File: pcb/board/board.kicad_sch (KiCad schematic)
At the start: 132 parts, among them J1 (A) USB_C_Receptacle_USB2.0_1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, J10 OLED_128x32, J11 LCD_128x160, J12 AudioJack3, J13 Conn_01x02, J14 Micro_SD_Card, J15 Conn_01x03, J16 Conn_01x06, J17 Conn_01x03, J18 Conn_01x03, J19 Conn_01x03, J2 (B) USB_C_Receptacle_USB2.0_1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, J20 Conn_01x04, J21 Conn_01x04, J22 Conn_01x05, J23 Conn_01x05, J24 Conn_01x05, J25 Conn_01x02, J3 (C) USB_C_Receptacle_USB2.0_1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, J4 Conn_01x03, J5 Conn_01x03, J6 Conn_01x04, J7 Conn_01x07, J8 Conn_01x04, J9 Conn_01x02, SW1 SW_Push, SW2 SW_Push, SW3 Switch, SW4 Switch, SW5 Switch, SW6 RotaryEncoder_Switch, U1 RP2040, U2 NCP1117-3.3_SOT223, U3 W25Q16JVZPIQ TR, U4 NCP1117-3.3_SOT223, U5 RP2040, U6 W25Q16JVZPIQ TR, U7 PCM5101A, U8 TLV70033_SOT23-5, U9 TPA6132A2RTE, Y1 12MHz, Y2 12MHz

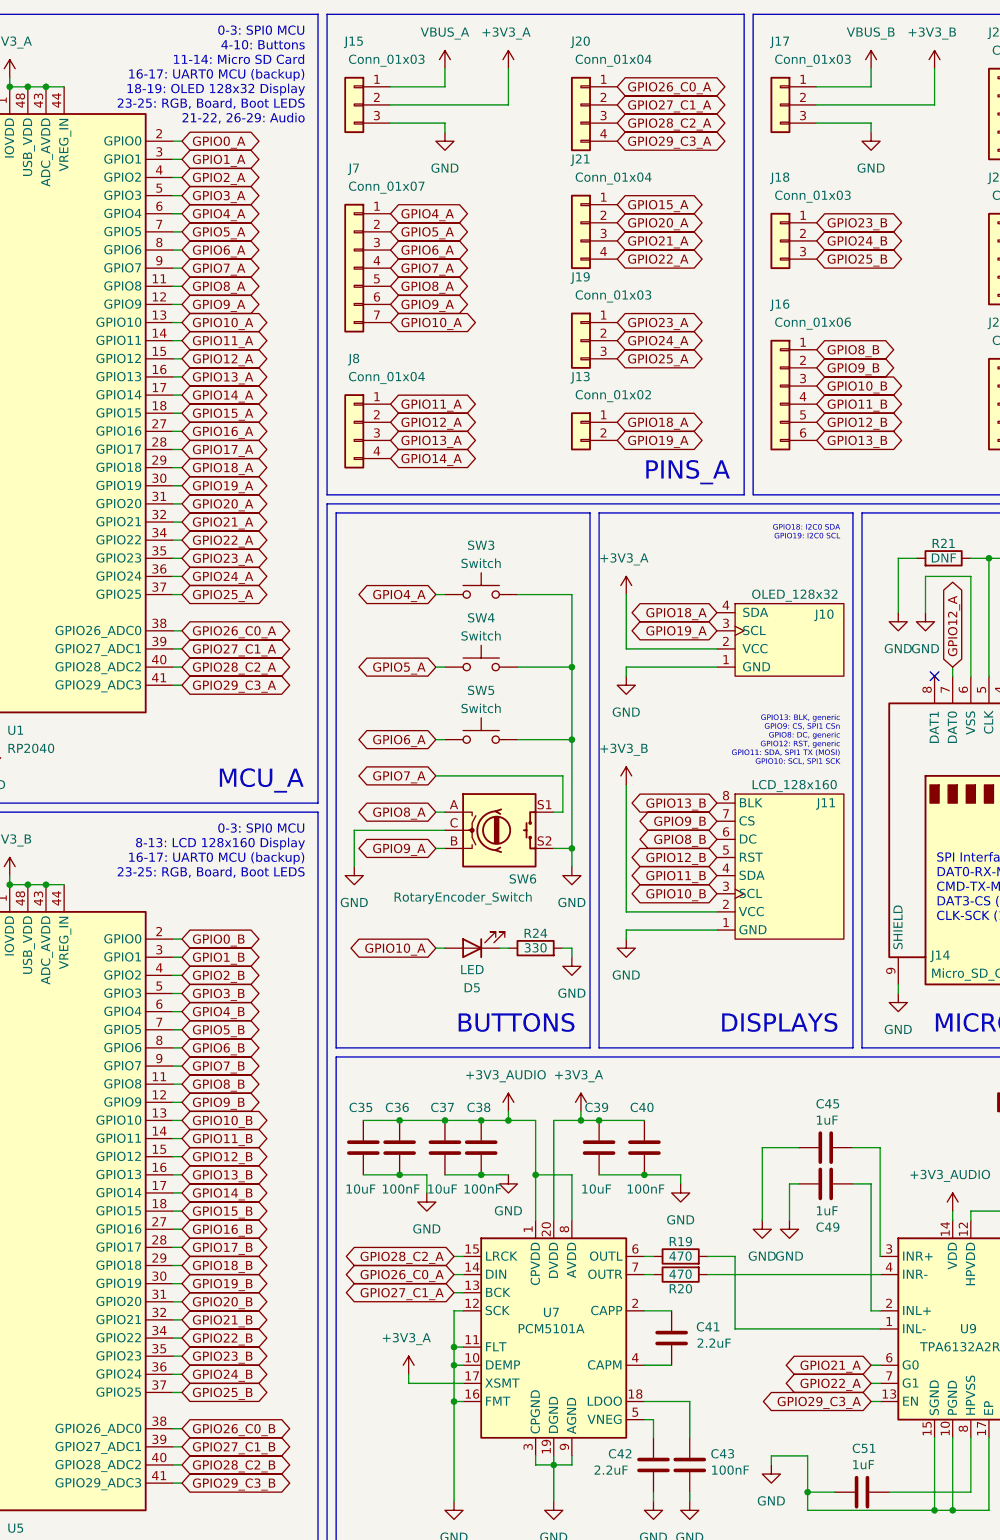
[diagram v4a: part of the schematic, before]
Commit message: 08172026 - pcb work continues! (audio and most mcu pin connections!)
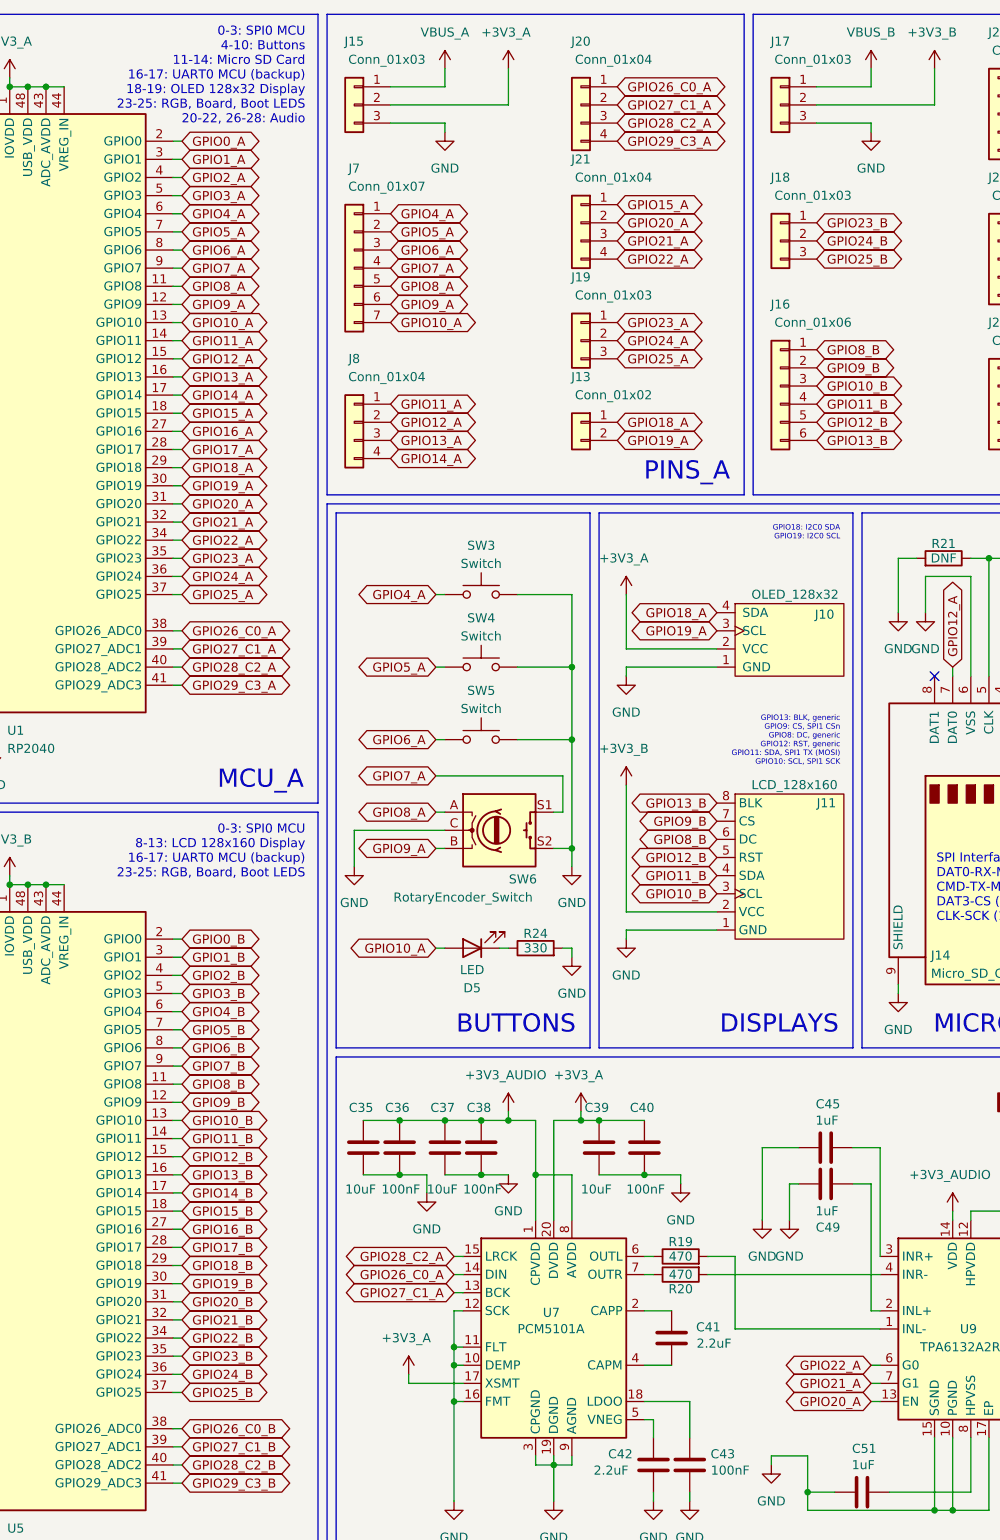
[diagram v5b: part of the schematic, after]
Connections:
- net GPIO20_A: now also U9.13 (EN)
- net GPIO21_A: now also U9.7 (G1); no longer U9.6 (G0)
- net GPIO22_A: now also U9.6 (G0); no longer U9.7 (G1)
- net GPIO29_C3_A: no longer U9.13 (EN)
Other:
- note added: "0-3: SPI0 MCU 4-10: Buttons 11-14: Micro SD Card 16-17: UART0 MCU (backup) 18-19: OLED 128x32 Display 23-25: RGB, Board, Boot LEDS 20-22, 26-28: Audio"
- note removed: "0-3: SPI0 MCU 4-10: Buttons 11-14: Micro SD Card 16-17: UART0 MCU (backup) 18-19: OLED 128x32 Display 23-25: RGB, Board, Boot LEDS 21-22, 26-29: Audio"
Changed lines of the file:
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@@
 	(wire
 		(pts
+			(xy 363.22 204.47) (xy 364.49 204.47)
+		)
+		(stroke
+			(width 0)
+			(type default)
+		)
+	)
+	(wire
+		(pts
 			(xy 163.83 144.78) (xy 170.18 144.78)
 		)
@@
 	(wire
 		(pts
+			(xy 363.22 207.01) (xy 364.49 207.01)
+		)
+		(stroke
+			(width 0)
+			(type default)
+		)
+	)
+	(wire
+		(pts
 			(xy 321.31 217.17) (xy 321.31 218.44)
 		)
@@
 	(wire
 		(pts
-			(xy 363.22 207.01) (xy 364.49 207.01)
-		)
-		(stroke
-			(width 0)
-			(type default)
-		)
-	)
-	(wire
-		(pts
 			(xy 69.85 144.78) (xy 69.85 143.51)
 		)
@@
 	(wire
 		(pts
-			(xy 363.22 204.47) (xy 364.49 204.47)
-		)
-		(stroke
-			(width 0)
-			(type default)
-		)
-	)
-	(wire
-		(pts
 			(xy 213.36 99.06) (xy 214.63 99.06)
 		)
@@
 		)
 	)
-	(text "0-3: SPI0 MCU\n4-10: Buttons\n11-14: Micro SD Card\n16-17: UART0 MCU (backup)\n18-19: OLED 128x32 Display\n23-25: RGB, Board, Boot LEDS\n21-22, 26-29: Audio"
+	(text "0-3: SPI0 MCU\n4-10: Buttons\n11-14: Micro SD Card\n16-17: UART0 MCU (backup)\n18-19: OLED 128x32 Display\n23-25: RGB, Board, Boot LEDS\n20-22, 26-28: Audio"
 		(exclude_from_sim no)
 		(at 283.972 17.018 0)
@@
 	(global_label "GPIO21_A"
 		(shape bidirectional)
-		(at 363.22 204.47 180)
+		(at 363.22 207.01 180)
 		(fields_autoplaced yes)
 		(effects
@@
 		)
 		(property "Intersheetrefs" "${INTERSHEET_REFS}"
-			(at 350.173 204.47 0)
+			(at 350.173 207.01 0)
 			(effects
 				(font
@@
 		)
 	)
+	(global_label "GPIO20_A"
+		(shape bidirectional)
+		(at 363.22 209.55 180)
+		(fields_autoplaced yes)
+		(effects
+			(font
+				(size 1.27 1.27)
+			)
+			(justify right)
+		)
+		(property "Intersheetrefs" "${INTERSHEET_REFS}"
+			(at 350.173 209.55 0)
+			(effects
+				(font
+					(size 1.27 1.27)
+				)
+				(justify right)
+				(hide yes)
+			)
+		)
+	)
 	(global_label "GPIO22_A"
 		(shape bidirectional)
@@
 		)
 	)
-	(global_label "GPIO29_C3_A"
-		(shape bidirectional)
-		(at 363.22 209.55 180)
-		(fields_autoplaced yes)
-		(effects
-			(font
-				(size 1.27 1.27)
-			)
-			(justify right)
-		)
-		(property "Intersheetrefs" "${INTERSHEET_REFS}"
-			(at 346.7259 209.55 0)
-			(effects
-				(font
-					(size 1.27 1.27)
-				)
-				(justify right)
-				(hide yes)
-			)
-		)
-	)
 	(global_label "GPIO7_B"
 		(shape bidirectional)
@@
 	(global_label "GPIO22_A"
 		(shape bidirectional)
-		(at 363.22 207.01 180)
+		(at 363.22 204.47 180)
 		(fields_autoplaced yes)
 		(effects
@@
 		)
 		(property "Intersheetrefs" "${INTERSHEET_REFS}"
-			(at 350.173 207.01 0)
+			(at 350.173 204.47 0)
 			(effects
 				(font

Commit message: leds and more connections!
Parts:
- removed J13: Conn_01x02, Connector_PinHeader_2.54mm:PinHeader_1x02_P2.54mm_Vertical, symbol Connector_Generic:Conn_01x02
- removed J15, J17, J18, J19: Conn_01x03, Connector_PinHeader_2.54mm:PinHeader_1x03_P2.54mm_Vertical, symbol Connector_Generic:Conn_01x03
- removed J16: Conn_01x06, Connector_PinHeader_2.54mm:PinHeader_1x06_P2.54mm_Vertical, symbol Connector_Generic:Conn_01x06
- removed J20, J21, J8: Conn_01x04, Connector_PinHeader_2.54mm:PinHeader_1x04_P2.54mm_Vertical, symbol Connector_Generic:Conn_01x04
- removed J22, J23, J24: Conn_01x05, Connector_PinHeader_2.54mm:PinHeader_1x05_P2.54mm_Vertical, symbol Connector_Generic:Conn_01x05
- removed J7: Conn_01x07, Connector_PinHeader_2.54mm:PinHeader_1x07_P2.54mm_Vertical, symbol Connector_Generic:Conn_01x07
- added J13, J7: Conn_01x01, TestPoint:TestPoint_Pad_1.0x1.0mm, symbol Connector_Generic:Conn_01x01
- added J15, J16, J8: Conn_01x01, Connector_PinHeader_2.54mm:PinHeader_1x01_P2.54mm_Vertical, symbol Connector_Generic:Conn_01x01
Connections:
- net +3V3_A: now also J8.1 (Pin_1)
- net +3V3_B: now also J15.1 (Pin_1)
- net GND: now also J16.1 (Pin_1)
- net VBUS_A: now also J7.1 (Pin_1)
- net VBUS_B: now also J13.1 (Pin_1)

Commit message: 08192026 - starting to wrap up pcb work!
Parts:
- removed J25, J9: Conn_01x02, Connector_PinHeader_2.54mm:PinHeader_1x02_P2.54mm_Vertical, symbol Connector_Generic:Conn_01x02
- removed J6: Conn_01x04, Connector_PinHeader_2.54mm:PinHeader_1x04_P2.54mm_Vertical, symbol Connector_Generic:Conn_01x04
- added J17, J18, J19, J20, J21, J22, J6, J9: Conn_01x01, TestPoint:TestPoint_Pad_D1.0mm, symbol Connector_Generic:Conn_01x01
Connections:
- net GPIO0_A: now also J6.1 (Pin_1)
- net GPIO0_B: now also J19.1 (Pin_1)
- net GPIO16_A: now also J9.1 (Pin_1)
- net GPIO16_B: now also J22.1 (Pin_1)
- net GPIO1_A: now also J17.1 (Pin_1)
- net GPIO2_A: now also J18.1 (Pin_1)
- net RUN_A: now also J20.1 (Pin_1)
- net RUN_B: now also J21.1 (Pin_1)

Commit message: 08232026 - exporting and back to again
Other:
- title: River Board -> River Board Schematic
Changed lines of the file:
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@@
 	(paper "A3")
 	(title_block
-		(title "River Board")
+		(title "River Board Schematic")
+		(date "2026-08-23")
 		(rev "1.0")
 		(company "HenryLi-0")
